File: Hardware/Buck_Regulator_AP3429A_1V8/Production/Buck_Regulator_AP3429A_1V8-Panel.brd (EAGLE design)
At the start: 226.8 x 169.2 mm, 2502 parts, among them J1 Screw Terminal, J10 Breakout Headers, J100 Breakout Headers, J101 Screw Terminal, J102 POWER_JACKPOWER_JACK_SLOT_COM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, J103 Breakout Headers, J104 Screw Terminal, J105 POWER_JACKPOWER_JACK_SLOT_COM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, J106 Breakout Headers, J107 Screw Terminal, J108 POWER_JACKPOWER_JACK_SLOT_COM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, J109 Breakout Headers, J11 Screw Terminal, J110 Screw Terminal, J111 POWER_JACKPOWER_JACK_SLOT_COM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, J112 Breakout Headers, J113 Screw Terminal, J114 POWER_JACKPOWER_JACK_SLOT_COM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, J115 Breakout Headers, J116 Screw Terminal, J117 POWER_JACKPOWER_JACK_SLOT_COM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, J118 Breakout Headers, J119 Screw Terminal, J12 POWER_JACKPOWER_JACK_SLOT_COM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, J120 POWER_JACKPOWER_JACK_SLOT_COM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, J121 Breakout Headers, J122 Screw Terminal, J123 POWER_JACKPOWER_JACK_SLOT_COM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, J124 Breakout Headers, J125 Screw Terminal, J126 POWER_JACKPOWER_JACK_SLOT_COM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, J127 Breakout Headers, J128 Screw Terminal, J129 POWER_JACKPOWER_JACK_SLOT_COM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, J13 Breakout Headers, J130 Breakout Headers, J131 Screw Terminal, J132 POWER_JACKPOWER_JACK_SLOT_COM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, J133 Breakout Headers, J134 Screw Terminal, J135 POWER_JACKPOWER_JACK_SLOT_COM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, J136 Breakout Headers, J137 Screw Terminal, J138 POWER_JACKPOWER_JACK_SLOT_COM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, J139 Breakout Headers, J14 Screw Terminal, J140 Screw Terminal, J141 POWER_JACKPOWER_JACK_SLOT_COM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, J142 Breakout Headers, J143 Screw Terminal, J144 POWER_JACKPOWER_JACK_SLOT_COM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, J15 POWER_JACKPOWER_JACK_SLOT_COM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, J16 Breakout Headers, J17 Screw Terminal, J18 POWER_JACKPOWER_JACK_SLOT_COM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, J19 Breakout Headers, J2 POWER_JACKPOWER_JACK_SLOT_COM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, J20 Screw Terminal, J21 POWER_JACKPOWER_JACK_SLOT_COM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, J22 Breakout Headers, J23 Screw Terminal, J24 POWER_JACKPOWER_JACK_SLOT_COM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, J25 Breakout Headers, J26 Screw Terminal, J27 POWER_JACKPOWER_JACK_SLOT_COM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, J28 Breakout Headers, J29 Screw Terminal, J3 Breakout Headers, J30 POWER_JACKPOWER_JACK_SLOT_COM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, J31 Breakout Headers, J32 Screw Terminal, J33 POWER_JACKPOWER_JACK_SLOT_COM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, J34 Breakout Headers, J35 Screw Terminal, J36 POWER_JACKPOWER_JACK_SLOT_COM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, J37 Breakout Headers, J38 Screw Terminal, J39 POWER_JACKPOWER_JACK_SLOT_COM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, J4 Breakout Headers, J40 Breakout Headers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

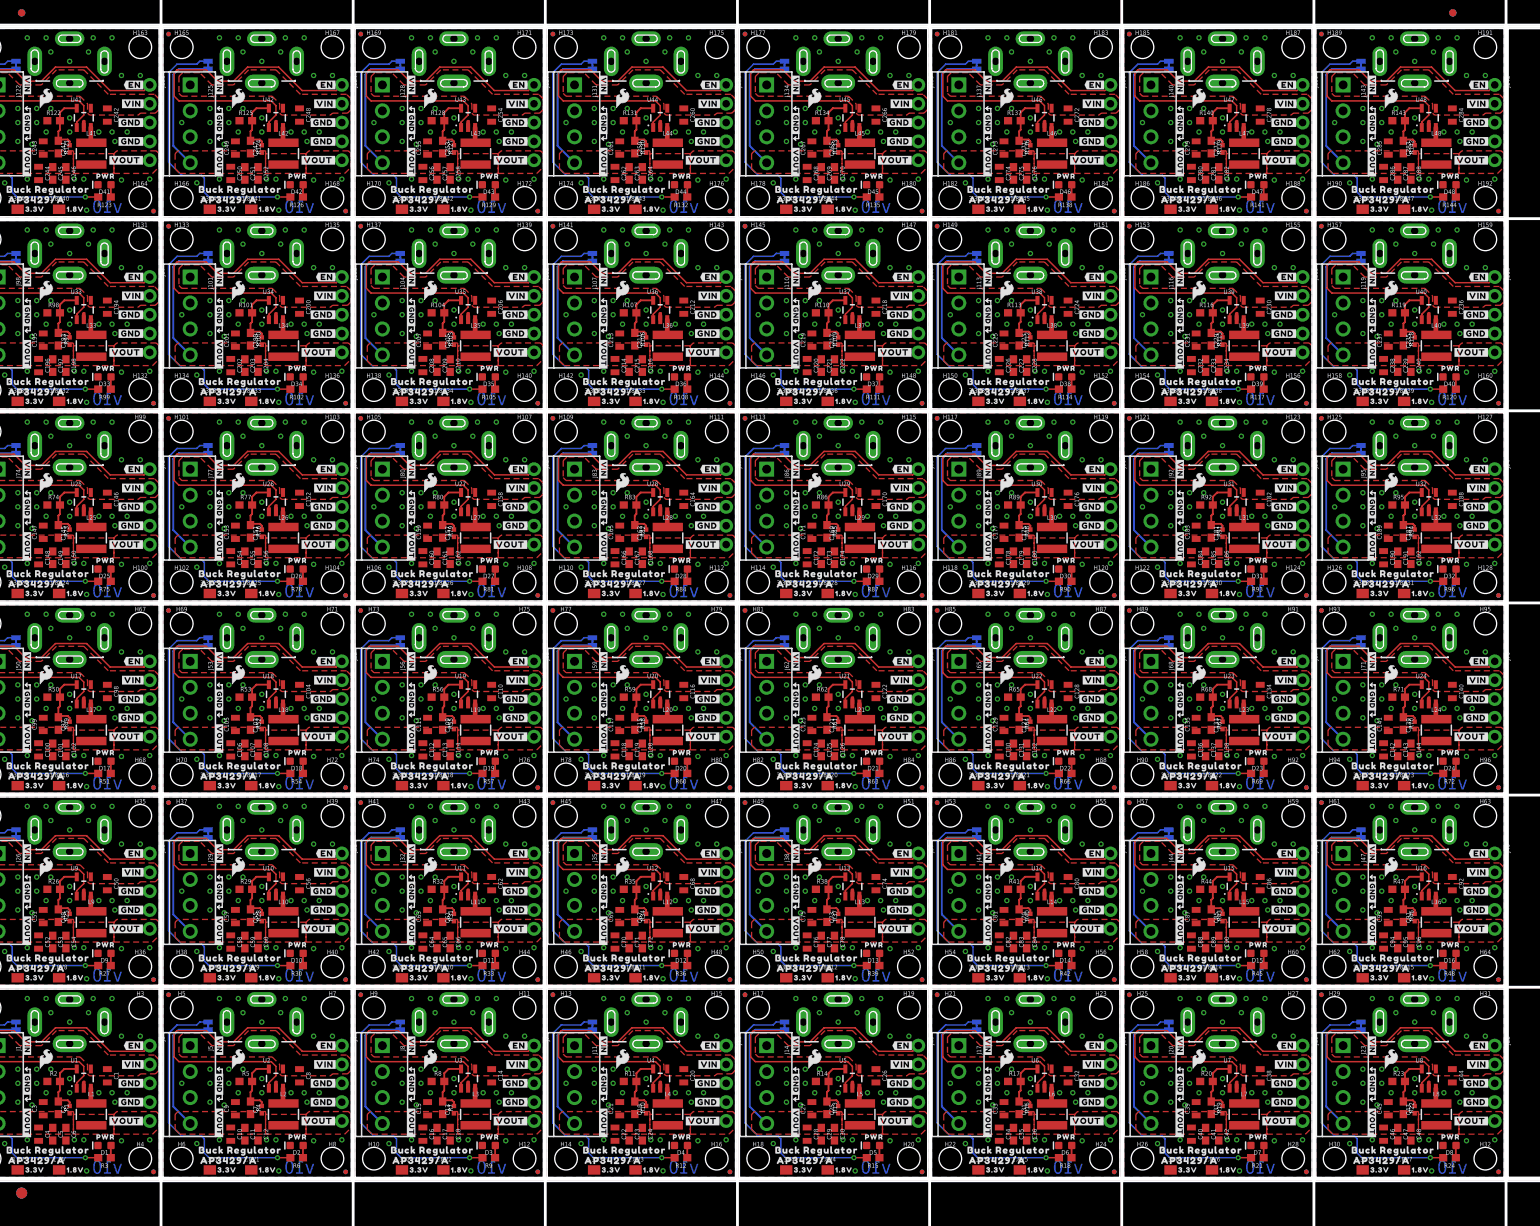
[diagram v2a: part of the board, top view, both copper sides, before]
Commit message: V11 Design Update
Added 100k resistor to pull EN high to VIN for an easier plug and play application.
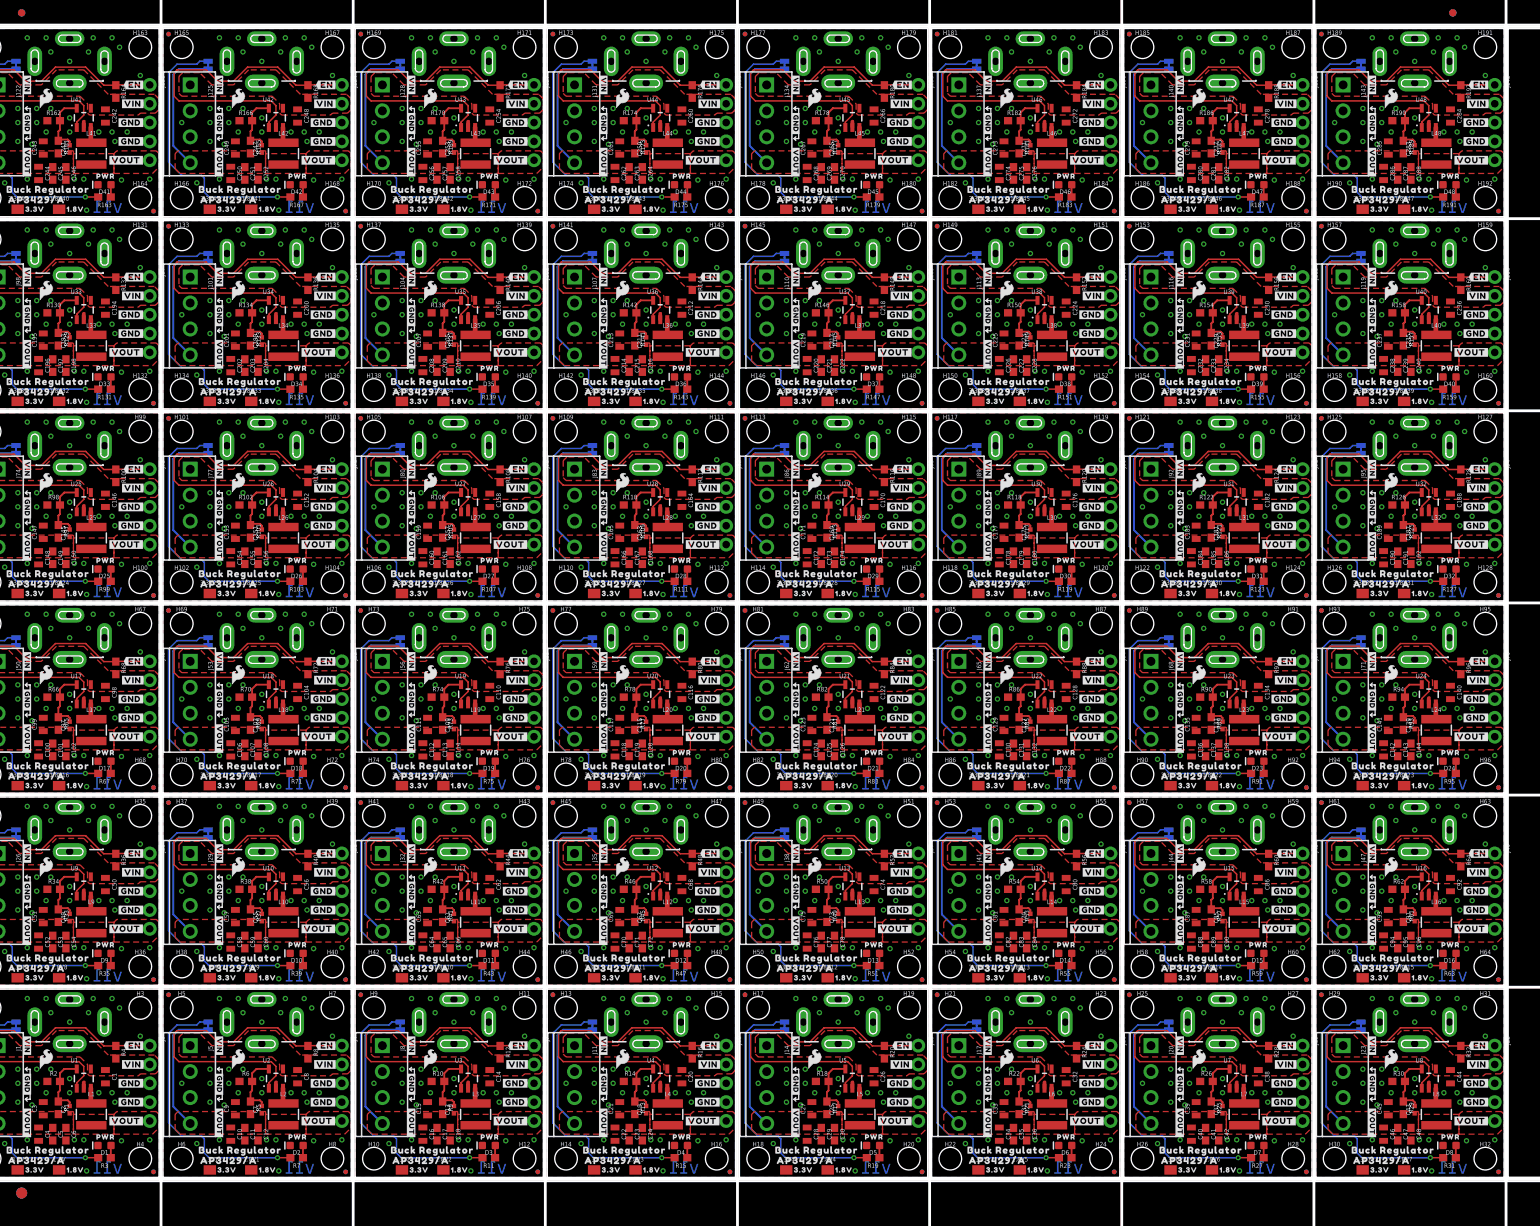
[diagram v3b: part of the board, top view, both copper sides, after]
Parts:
- added R145, R149, R153, R157, R161, R165, R169, R173, R177, R181, R185, R189: 300k, SparkFun-Resistors:0603
- added R146, R150, R154, R158, R162, R166, R170, R174, R178, R182, R186, R190: 150k, SparkFun-Resistors:0603
- added R147, R151, R155, R159, R163, R167, R171, R175, R179, R183, R187, R191: 100, SparkFun-Resistors:0603
- added R148, R152, R156, R160, R164, R168, R172, R176, R180, R184, R188, R192: 100k, SparkFun-Resistors:0603
- R10, R106, R118, R130, R142, R22, R34, R46, R58, R70, R82, R94: value 300k -> 150k
- R100, R112, R124, R136, R16, R28, R4, R40, R52, R64, R76, R88: value 300k -> 100k
- R101, R113, R125, R137, R17, R29, R41, R5, R53, R65, R77, R89: value 150k -> 300k
- R102, R114, R126, R138, R18, R30, R42, R54, R6, R66, R78, R90: value 100 -> 150k
- R103, R115, R127, R139, R19, R31, R43, R55, R67, R7, R79, R91: value 300k -> 100
- R104, R116, R128, R140, R20, R32, R44, R56, R68, R8, R80, R92: value 150k -> 100k
- R105, R117, R129, R141, R21, R33, R45, R57, R69, R81, R9, R93: value 100 -> 300k
- R107, R11, R119, R131, R143, R23, R35, R47, R59, R71, R83, R95: value 150k -> 100
- R108, R12, R120, R132, R144, R24, R36, R48, R60, R72, R84, R96: value 100 -> 100k
- moved R125 165.6 mm to (193.2, 87.1), turned to 270 degrees
- moved R122 163.9 mm to (166.6, 90.7)
- moved R123 163.9 mm to (173.5, 80.4)
- moved R121 163.9 mm to (167.3, 87.1)
- moved R29 158.8 mm to (193.2, 9.40), turned to 270 degrees
- moved R26 157.6 mm to (166.6, 13.0)
- moved R27 157.6 mm to (173.5, 2.67)
- moved R25 157.6 mm to (167.3, 9.40)
- moved R70 156.1 mm to (37.1, 64.8), turned to 0 degrees
- moved R72 154.6 mm to (45.5, 68.7), turned to 270 degrees
- moved R126 154.3 mm to (192.5, 90.7), turned to 0 degrees
- moved R30 149.4 mm to (192.5, 13.0), turned to 0 degrees
- moved R67 149.4 mm to (18.0, 54.5), turned to 180 degrees
- moved R71 148.9 mm to (43.9, 54.5), turned to 180 degrees
- moved R127 147.8 mm to (199.4, 80.4), turned to 180 degrees
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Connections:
- net EN: now also R4.1
- net EN1: now also R8.1
- net EN10: now also R44.1
- net EN11: now also R48.1
- net EN12: now also R52.1
- net EN13: now also R56.1
- net EN14: now also R60.1
- net EN15: now also R64.1
- net EN16: now also R68.1
- net EN17: now also R72.1
- net EN18: now also R76.1
- net EN19: now also R80.1
- net EN2: now also R12.1
- net EN20: now also R84.1
- net EN21: now also R88.1
- net EN22: now also R92.1
- net EN23: now also R96.1
- net EN24: now also R100.1
- net EN25: now also R104.1
- net EN26: now also R108.1
- net EN27: now also R112.1
- net EN28: now also R116.1
- net EN29: now also R120.1
- net EN3: now also R16.1
- net EN30: now also R124.1
- net EN31: now also R128.1
- net EN32: now also R132.1
- net EN33: now also R136.1
- net EN34: now also R140.1
- net EN35: now also R144.1
- net EN36: now also R148.1
- net EN37: now also R152.1
- net EN38: now also R156.1
- net EN39: now also R160.1
- net EN4: now also R20.1
- net EN40: now also R164.1
- net EN41: now also R168.1
- net EN42: now also R172.1
- net EN43: now also R176.1
- net EN44: now also R180.1
- net EN45: now also R184.1
- net EN46: now also R188.1
- net EN47: now also R192.1
- net EN5: now also R24.1
- net EN6: now also R28.1
- net EN7: now also R32.1
- net EN8: now also R36.1
- net EN9: now also R40.1
- net GND1: now also R6.1; no longer R5.1
- net GND10: now also R42.1; no longer R32.1
- net GND11: now also R46.1; no longer R35.1
- net GND12: now also R50.1; no longer R38.1
- net GND13: now also R54.1; no longer R41.1
- net GND14: now also R58.1; no longer R44.1
- net GND15: now also R62.1; no longer R47.1
- net GND16: now also R66.1; no longer R50.1
- net GND17: now also R70.1; no longer R53.1
- net GND18: now also R74.1; no longer R56.1
- net GND19: now also R78.1; no longer R59.1
- net GND2: now also R10.1; no longer R8.1
- net GND20: now also R82.1; no longer R62.1
- net GND21: now also R86.1; no longer R65.1
- net GND22: now also R90.1; no longer R68.1
- net GND23: now also R94.1; no longer R71.1
- net GND24: now also R98.1; no longer R74.1
- net GND25: now also R102.1; no longer R77.1
- net GND26: now also R106.1; no longer R80.1
- net GND27: now also R110.1; no longer R83.1
- net GND28: now also R114.1; no longer R86.1
- net GND29: now also R118.1; no longer R89.1
- net GND3: now also R14.1; no longer R11.1
- net GND30: now also R122.1; no longer R92.1
- net GND31: now also R126.1; no longer R95.1
- net GND32: now also R130.1; no longer R98.1
- net GND33: now also R134.1; no longer R101.1
- net GND34: now also R138.1; no longer R104.1
- net GND35: now also R142.1; no longer R107.1
- net GND36: now also R146.1; no longer R110.1
- net GND37: now also R150.1; no longer R113.1
- net GND38: now also R154.1; no longer R116.1
- net GND39: now also R158.1; no longer R119.1
- net GND4: now also R18.1; no longer R14.1
- net GND40: now also R162.1; no longer R122.1
- net GND41: now also R166.1; no longer R125.1
- net GND42: now also R170.1; no longer R128.1
- net GND43: now also R174.1; no longer R131.1
- net GND44: now also R178.1; no longer R134.1
- net GND45: now also R182.1; no longer R137.1
- net GND46: now also R186.1; no longer R140.1
- net GND47: now also R190.1; no longer R143.1
- net GND5: now also R22.1; no longer R17.1
- net GND6: now also R26.1; no longer R20.1
- net GND7: now also R30.1; no longer R23.1
- net GND8: now also R34.1; no longer R26.1
- net GND9: now also R38.1; no longer R29.1
- net N$10: now also R10.2, R9.1; no longer R7.1, R8.2
- net N$100: now also R99.1; no longer R75.1
- net N$102: now also R101.1, R102.2; no longer R76.1, R77.2
- net N$103: now also R103.2; no longer R78.2
- net N$104: now also R103.1; no longer R78.1
- net N$106: now also R105.1, R106.2; no longer R79.1, R80.2
- net N$107: now also R107.2; no longer R81.2
- net N$108: now also R107.1; no longer R81.1
- net N$11: now also R11.2; no longer R9.2
- net N$110: now also R109.1, R110.2; no longer R82.1, R83.2
- net N$111: now also R111.2; no longer R84.2
- net N$112: now also R111.1; no longer R84.1
- net N$114: now also R113.1, R114.2; no longer R85.1, R86.2
- net N$115: now also R115.2; no longer R87.2
- net N$116: now also R115.1; no longer R87.1
- net N$118: now also R117.1, R118.2; no longer R88.1, R89.2
- net N$119: now also R119.2; no longer R90.2
- net N$12: now also R11.1; no longer R9.1
- net N$120: now also R119.1; no longer R90.1
- net N$122: now also R121.1, R122.2; no longer R91.1, R92.2
- net N$123: now also R123.2; no longer R93.2
- net N$124: now also R123.1; no longer R93.1
- net N$126: now also R125.1, R126.2; no longer R94.1, R95.2
- net N$127: now also R127.2; no longer R96.2
- net N$128: now also R127.1; no longer R96.1
- net N$130: now also R129.1, R130.2; no longer R97.1, R98.2
- net N$131: now also R131.2; no longer R99.2
- net N$132: now also R131.1; no longer R99.1
- net N$134: now also R133.1, R134.2; no longer R100.1, R101.2
- net N$135: now also R135.2; no longer R102.2
- net N$136: now also R135.1; no longer R102.1
- net N$138: now also R137.1, R138.2; no longer R103.1, R104.2
- net N$139: now also R139.2; no longer R105.2
- net N$14: now also R13.1, R14.2; no longer R10.1, R11.2
- net N$140: now also R139.1; no longer R105.1
- net N$142: now also R141.1, R142.2; no longer R106.1, R107.2
- net N$143: now also R143.2; no longer R108.2
- net N$144: now also R143.1; no longer R108.1
- net N$146: now also R145.1, R146.2; no longer R109.1, R110.2
- net N$147: now also R147.2; no longer R111.2
- net N$148: now also R147.1; no longer R111.1
- net N$15: now also R15.2; no longer R12.2
- net N$150: now also R149.1, R150.2; no longer R112.1, R113.2
- net N$151: now also R151.2; no longer R114.2
- net N$152: now also R151.1; no longer R114.1
- net N$154: now also R153.1, R154.2; no longer R115.1, R116.2
- net N$155: now also R155.2; no longer R117.2
- net N$156: now also R155.1; no longer R117.1
- net N$158: now also R157.1, R158.2; no longer R118.1, R119.2
- net N$159: now also R159.2; no longer R120.2
- net N$16: now also R15.1; no longer R12.1
- net N$160: now also R159.1; no longer R120.1
- net N$162: now also R161.1, R162.2; no longer R121.1, R122.2
- net N$163: now also R163.2; no longer R123.2
- net N$164: now also R163.1; no longer R123.1
- net N$166: now also R165.1, R166.2; no longer R124.1, R125.2
- net N$167: now also R167.2; no longer R126.2
- net N$168: now also R167.1; no longer R126.1
- net N$170: now also R169.1, R170.2; no longer R127.1, R128.2
- net N$171: now also R171.2; no longer R129.2
- net N$172: now also R171.1; no longer R129.1
- net N$174: now also R173.1, R174.2; no longer R130.1, R131.2
- net N$175: now also R175.2; no longer R132.2
- net N$176: now also R175.1; no longer R132.1
- net N$178: now also R177.1, R178.2; no longer R133.1, R134.2
- net N$179: now also R179.2; no longer R135.2
- net N$18: now also R17.1, R18.2; no longer R13.1, R14.2
- net N$180: now also R179.1; no longer R135.1
- net N$182: now also R181.1, R182.2; no longer R136.1, R137.2
- net N$183: now also R183.2; no longer R138.2
- net N$184: now also R183.1; no longer R138.1
- net N$186: now also R185.1, R186.2; no longer R139.1, R140.2
- net N$187: now also R187.2; no longer R141.2
- net N$188: now also R187.1; no longer R141.1
- net N$19: now also R19.2; no longer R15.2
- net N$190: now also R189.1, R190.2; no longer R142.1, R143.2
- net N$191: now also R191.2; no longer R144.2
- net N$192: now also R191.1; no longer R144.1
- net N$20: now also R19.1; no longer R15.1
- net N$22: now also R21.1, R22.2; no longer R16.1, R17.2
- net N$23: now also R23.2; no longer R18.2
- net N$24: now also R23.1; no longer R18.1
- net N$26: now also R25.1, R26.2; no longer R19.1, R20.2
- net N$27: now also R27.2; no longer R21.2
- net N$28: now also R27.1; no longer R21.1
- net N$30: now also R29.1, R30.2; no longer R22.1, R23.2
- net N$31: now also R31.2; no longer R24.2
- net N$32: now also R31.1; no longer R24.1
- net N$34: now also R33.1, R34.2; no longer R25.1, R26.2
- net N$35: now also R35.2; no longer R27.2
- net N$36: now also R35.1; no longer R27.1
- net N$38: now also R37.1, R38.2; no longer R28.1, R29.2
- net N$39: now also R39.2; no longer R30.2
- net N$40: now also R39.1; no longer R30.1
- net N$42: now also R41.1, R42.2; no longer R31.1, R32.2
- net N$43: now also R43.2; no longer R33.2
- net N$44: now also R43.1; no longer R33.1
- net N$46: now also R45.1, R46.2; no longer R34.1, R35.2
- net N$47: now also R47.2; no longer R36.2
- net N$48: now also R47.1; no longer R36.1
- net N$50: now also R49.1, R50.2; no longer R37.1, R38.2
- net N$51: now also R51.2; no longer R39.2
- net N$52: now also R51.1; no longer R39.1
- net N$54: now also R53.1, R54.2; no longer R40.1, R41.2
- net N$55: now also R55.2; no longer R42.2
- net N$56: now also R55.1; no longer R42.1
- net N$58: now also R57.1, R58.2; no longer R43.1, R44.2
- net N$59: now also R59.2; no longer R45.2
- net N$6: now also R5.1, R6.2; no longer R4.1, R5.2
- net N$60: now also R59.1; no longer R45.1
- net N$62: now also R61.1, R62.2; no longer R46.1, R47.2
- net N$63: now also R63.2; no longer R48.2
- net N$64: now also R63.1; no longer R48.1
- net N$66: now also R65.1, R66.2; no longer R49.1, R50.2
- net N$67: now also R67.2; no longer R51.2
- net N$68: now also R67.1; no longer R51.1
- net N$7: now also R7.2; no longer R6.2
- net N$70: now also R69.1, R70.2; no longer R52.1, R53.2
- net N$71: now also R71.2; no longer R54.2
- net N$72: now also R71.1; no longer R54.1
- net N$74: now also R73.1, R74.2; no longer R55.1, R56.2
- net N$75: now also R75.2; no longer R57.2
- net N$76: now also R75.1; no longer R57.1
- net N$78: now also R77.1, R78.2; no longer R58.1, R59.2
- net N$79: now also R79.2; no longer R60.2
- net N$8: now also R7.1; no longer R6.1
- net N$80: now also R79.1; no longer R60.1
- net N$82: now also R81.1, R82.2; no longer R61.1, R62.2
- net N$83: now also R83.2; no longer R63.2
- net N$84: now also R83.1; no longer R63.1
- net N$86: now also R85.1, R86.2; no longer R64.1, R65.2
- net N$87: now also R87.2; no longer R66.2
- net N$88: now also R87.1; no longer R66.1
- net N$90: now also R89.1, R90.2; no longer R67.1, R68.2
- net N$91: now also R91.2; no longer R69.2
- net N$92: now also R91.1; no longer R69.1
- net N$94: now also R93.1, R94.2; no longer R70.1, R71.2
- net N$95: now also R95.2; no longer R72.2
- net N$96: now also R95.1; no longer R72.1
- net N$98: now also R97.1, R98.2; no longer R73.1, R74.2
- net N$99: now also R99.2; no longer R75.2
- net VIN: now also R4.2
- net VIN1: now also R8.2
- net VIN10: now also R44.2
- net VIN11: now also R48.2
- net VIN12: now also R52.2
- net VIN13: now also R56.2
- net VIN14: now also R60.2
- net VIN15: now also R64.2
- net VIN16: now also R68.2
- net VIN17: now also R72.2
- net VIN18: now also R76.2
- net VIN19: now also R80.2
- net VIN2: now also R12.2
- net VIN20: now also R84.2
- net VIN21: now also R88.2
- net VIN22: now also R92.2
- net VIN23: now also R96.2
- net VIN24: now also R100.2
- net VIN25: now also R104.2
- net VIN26: now also R108.2
- net VIN27: now also R112.2
- net VIN28: now also R116.2
- net VIN29: now also R120.2
- net VIN3: now also R16.2
- net VIN30: now also R124.2
- net VIN31: now also R128.2
- net VIN32: now also R132.2
- net VIN33: now also R136.2
- net VIN34: now also R140.2
- net VIN35: now also R144.2
- net VIN36: now also R148.2
- net VIN37: now also R152.2
- net VIN38: now also R156.2
- net VIN39: now also R160.2
- net VIN4: now also R20.2
- net VIN40: now also R164.2
- net VIN41: now also R168.2
- net VIN42: now also R172.2
- net VIN43: now also R176.2
- net VIN44: now also R180.2
- net VIN45: now also R184.2
- net VIN46: now also R188.2
- net VIN47: now also R192.2
- net VIN5: now also R24.2
- net VIN6: now also R28.2
- net VIN7: now also R32.2
- net VIN8: now also R36.2
- net VIN9: now also R40.2
- net VOUT1: now also R5.2; no longer R4.2
- net VOUT10: now also R41.2; no longer R31.2
- net VOUT11: now also R45.2; no longer R34.2
- net VOUT12: now also R49.2; no longer R37.2
- net VOUT13: now also R53.2; no longer R40.2
- net VOUT14: now also R57.2; no longer R43.2
- net VOUT15: now also R61.2; no longer R46.2
- net VOUT16: now also R65.2; no longer R49.2
- net VOUT17: now also R69.2; no longer R52.2
- net VOUT18: now also R73.2; no longer R55.2
- net VOUT19: now also R77.2; no longer R58.2
- net VOUT2: now also R9.2; no longer R7.2
- net VOUT20: now also R81.2; no longer R61.2
- net VOUT21: now also R85.2; no longer R64.2
- net VOUT22: now also R89.2; no longer R67.2
- net VOUT23: now also R93.2; no longer R70.2
- net VOUT24: now also R97.2; no longer R73.2
- net VOUT25: now also R101.2; no longer R76.2
- net VOUT26: now also R105.2; no longer R79.2
- net VOUT27: now also R109.2; no longer R82.2
- net VOUT28: now also R113.2; no longer R85.2
- net VOUT29: now also R117.2; no longer R88.2
- net VOUT3: now also R13.2; no longer R10.2
- net VOUT30: now also R121.2; no longer R91.2
- net VOUT31: now also R125.2; no longer R94.2
- net VOUT32: now also R129.2; no longer R97.2
- net VOUT33: now also R133.2; no longer R100.2
- net VOUT34: now also R137.2; no longer R103.2
- net VOUT35: now also R141.2; no longer R106.2
- net VOUT36: now also R145.2; no longer R109.2
- net VOUT37: now also R149.2; no longer R112.2
- net VOUT38: now also R153.2; no longer R115.2
- net VOUT39: now also R157.2; no longer R118.2
- net VOUT4: now also R17.2; no longer R13.2
- net VOUT40: now also R161.2; no longer R121.2
- net VOUT41: now also R165.2; no longer R124.2
- net VOUT42: now also R169.2; no longer R127.2
- net VOUT43: now also R173.2; no longer R130.2
- net VOUT44: now also R177.2; no longer R133.2
- net VOUT45: now also R181.2; no longer R136.2
- net VOUT46: now also R185.2; no longer R139.2
- net VOUT47: now also R189.2; no longer R142.2
- net VOUT5: now also R21.2; no longer R16.2
- net VOUT6: now also R25.2; no longer R19.2
- net VOUT7: now also R29.2; no longer R22.2
- net VOUT8: now also R33.2; no longer R25.2
- net VOUT9: now also R37.2; no longer R28.2
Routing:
- net EN46: track 46.6 -> 46.0 mm
- net EN45: track 46.6 -> 46.0 mm
- net EN42: track 46.6 -> 46.0 mm
- net EN41: track 46.6 -> 46.0 mm
- net EN47: track 46.6 -> 46.0 mm
- net EN44: track 46.6 -> 46.0 mm
- net EN43: track 46.6 -> 46.0 mm
- net EN40: track 46.6 -> 46.0 mm
- net EN7: track 46.6 -> 46.0 mm
- net EN4: track 46.6 -> 46.0 mm
- net EN39: track 46.6 -> 46.0 mm
- net EN30: track 46.6 -> 46.0 mm
- net EN3: track 46.6 -> 46.0 mm
- net EN26: track 46.6 -> 46.0 mm
- net EN2: track 46.6 -> 46.0 mm
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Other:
- board text added: "v11"
- board text removed: "v10"
